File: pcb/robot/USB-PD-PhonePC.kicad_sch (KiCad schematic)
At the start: 1 part, among them J9 Conn_01x16

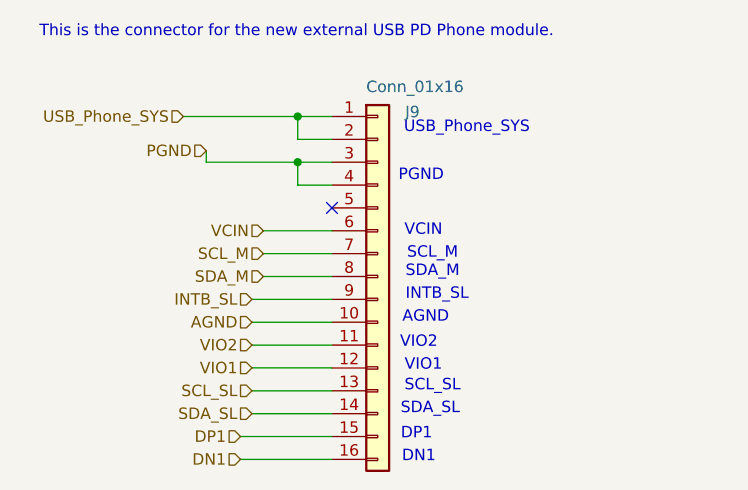
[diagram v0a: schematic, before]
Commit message: Add removable I2C isolation jumpers on i2c0 and i2c1 (fixes #18)
Add a 0-ohm series resistor on both SDA and SCL for each slave on the
shared I2C buses, so a specific device can be isolated during
debugging (bus lockup / SDA-held-low) by pulling one resistor instead
of physical rework.

i2c0: R32/R33 (U1, STWLC38), R34/R35 (U12, fuel gauge), R36/R37 (U8,
motor driver), R38/R39 (U9, motor driver), R40/R53 (U6, MAX77857 -
placed between the level-shifter U5 and U6 so it isolates only that
branch). J9's existing link to the USB-PD module (R6/R7) was already
covered, no new jumper needed there.

i2c1: R55/R57 (U13, MAX77976 charger) and R65/R73 (J9's other I2C
link to the USB-PD module) - extended to this bus too, not just
i2c0 as the issue literally named, since the same lockup risk applies.

All 10 are 0-ohm, 0603, populated by default - only pull the one for
the suspect device during debugging. Placed for hand accessibility
where board space allowed.

Verified via ERC/DRC against the pre-#18 baseline: 0 unconnected
items, no new violations (318 ERC / 27 DRC, unchanged).

Co-Authored-By: Claude Sonnet 5 <noreply@anthropic.com>
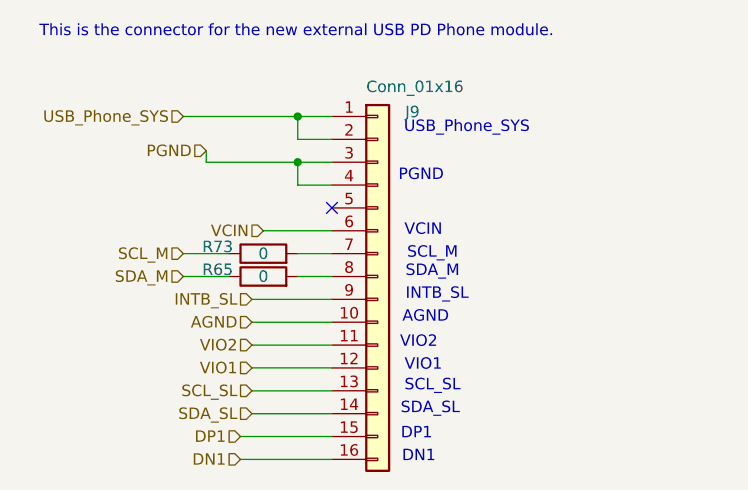
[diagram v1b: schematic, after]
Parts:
- added R65, R73: 0, robot:R_0603_1608Metric, symbol Device:R
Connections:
- net SCL_M: now also R73.1; no longer J9.7 (Pin_7)
- net SDA_M: now also R65.1; no longer J9.8 (Pin_8)
- new net: J9.7 (Pin_7), R73.2
- new net: J9.8 (Pin_8), R65.2
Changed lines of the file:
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@@
+	(wire
+		(pts
+			(xy 276.86 200.66) (xy 281.94 200.66)
+		)
+		(stroke
+			(width 0)
+			(type default)
+		)
+	)
+	(wire
+		(pts
+			(xy 289.56 203.2) (xy 293.37 203.2)
+		)
+		(stroke
+			(width 0)
+			(type default)
+		)
+	)
 	(wire
 		(pts
@@
 	(wire
 		(pts
-			(xy 285.75 203.2) (xy 293.37 203.2)
-		)
-		(stroke
-			(width 0)
-			(type default)
-		)
-	)
-	(wire
-		(pts
-			(xy 285.75 200.66) (xy 293.37 200.66)
-		)
-		(stroke
-			(width 0)
-			(type default)
-		)
-	)
-	(wire
-		(pts
 			(xy 283.21 223.52) (xy 293.37 223.52)
 		)
@@
 	(wire
 		(pts
+			(xy 289.56 200.66) (xy 293.37 200.66)
+		)
+		(stroke
+			(width 0)
+			(type default)
+		)
+	)
+	(wire
+		(pts
 			(xy 284.48 210.82) (xy 293.37 210.82)
 		)
@@
 	(wire
 		(pts
+			(xy 276.86 203.2) (xy 281.94 203.2)
+		)
+		(stroke
+			(width 0)
+			(type default)
+		)
+	)
+	(wire
+		(pts
 			(xy 289.56 190.5) (xy 279.4 190.5)
 		)
@@
 	(hierarchical_label "SDA_M"
 		(shape input)
-		(at 285.75 203.2 180)
+		(at 276.86 203.2 180)
 		(effects
 			(font
@@
 	(hierarchical_label "SCL_M"
 		(shape input)
-		(at 285.75 200.66 180)
+		(at 276.86 200.66 180)
 		(effects
 			(font
@@
 					(unit 1)
 				)
+			)
+		)
+	)
+	(symbol
+		(lib_id "Device:R")
+		(at 285.75 203.2 90)
+		(unit 1)
+		(exclude_from_sim no)
+		(in_bom yes)
+		(on_board yes)
+		(dnp no)
+		(property "Reference" "R65"
+			(at 280.67 202.438 90)
+			(effects
+				(font
+					(size 1.27 1.27)
+				)
+			)
+		)
+		(property "Value" "0"
+			(at 285.75 203.2 90)
+			(effects
+				(font
+					(size 1.27 1.27)
+				)
+			)
+		)
+		(property "Footprint" "robot:R_0603_1608Metric"
+			(at 285.75 204.978 90)
+			(effects
+				(font
+					(size 1.27 1.27)
+				)
+				(hide yes)
+			)
+		)
+		(property "Datasheet" "~"
+			(at 285.75 203.2 0)
+			(effects
+				(font
+					(size 1.27 1.27)
+				)
+				(hide yes)
+			)
+		)
+		(property "Description" ""
+			(at 285.75 203.2 0)
+			(effects
+				(font
+					(size 1.27 1.27)
+				)
+			)
+		)
+		(property "Manufacturer" "Stackpole Electronics"
+			(at 285.75 203.2 90)
+			(effects
+				(font
+					(size 1.27 1.27)
+				)
+				(hide yes)
+			)
+		)
+		(property "Part Number" "RMCF0603ZT0R00"
+			(at 285.75 203.2 90)
+			(effects
+				(font
+					(size 1.27 1.27)
+				)
+				(hide yes)
+			)
+		)
+		(property "Stock" "15"
+			(at 285.75 203.2 0)
+			(effects
+				(font
+					(size 1.27 1.27)
+				)
+				(hide yes)
+			)
+		)
+		(property "Type" "SMD"
+			(at 285.75 203.2 0)
+			(effects
+				(font
+					(size 1.27 1.27)
+				)
+				(hide yes)
+			)
+		)
+		(pin "1"
+		)
+		(pin "2"
+		)
+		(instances
+			(project "robot"
+				(path "/0c7b298e-2d07-4b1f-b033-e95f02d45089/b1182274-8387-45c9-b9a4-abcd767ed6f2"
+					(reference "R65")
+					(unit 1)
+				)
+			)
+		)
+	)
+	(symbol
+		(lib_id "Device:R")
+		(at 285.75 200.66 90)
+		(unit 1)
+		(exclude_from_sim no)
+		(in_bom yes)
+		(on_board yes)
+		(dnp no)
+		(property "Reference" "R73"
+			(at 280.67 199.898 90)
+			(effects
+				(font
+					(size 1.27 1.27)
+				)
+			)
+		)
+		(property "Value" "0"
+			(at 285.75 200.66 90)
+			(effects
+				(font
+					(size 1.27 1.27)
+				)
+			)
+		)
+		(property "Footprint" "robot:R_0603_1608Metric"
+			(at 285.75 202.438 90)
+			(effects
+				(font
+					(size 1.27 1.27)
+				)
+				(hide yes)
+			)
+		)
+		(property "Datasheet" "~"
+			(at 285.75 200.66 0)
+			(effects
+				(font
+					(size 1.27 1.27)
+				)
+				(hide yes)
+			)
+		)
+		(property "Description" ""
+			(at 285.75 200.66 0)
+			(effects
+				(font
+					(size 1.27 1.27)
+				)
+			)
+		)
+		(property "Manufacturer" "Stackpole Electronics"
+			(at 285.75 200.66 90)
+			(effects
+				(font
+					(size 1.27 1.27)
+				)
+				(hide yes)
+			)
+		)
+		(property "Part Number" "RMCF0603ZT0R00"
+			(at 285.75 200.66 90)
+			(effects
+				(font
+					(size 1.27 1.27)
+				)
+				(hide yes)
+			)
+		)
+		(property "Stock" "15"
+			(at 285.75 200.66 0)
+			(effects
+				(font
+					(size 1.27 1.27)
+				)
+				(hide yes)
+			)
+		)
+		(property "Type" "SMD"
+			(at 285.75 200.66 0)
+			(effects
+				(font
+					(size 1.27 1.27)
+				)
+				(hide yes)
+			)
+		)
+		(pin "1"
+		)
+		(pin "2"
+		)
+		(instances
+			(project "robot"
+				(path "/0c7b298e-2d07-4b1f-b033-e95f02d45089/b1182274-8387-45c9-b9a4-abcd767ed6f2"
+					(reference "R73")
+					(unit 1)
+				)
